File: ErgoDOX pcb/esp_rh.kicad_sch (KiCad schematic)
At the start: 6 parts

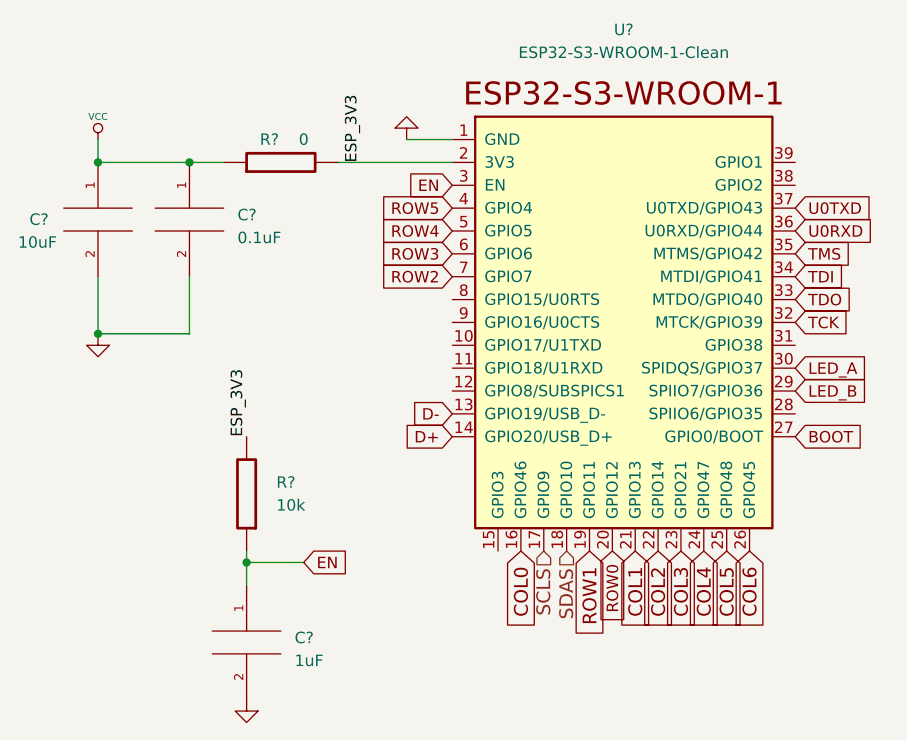
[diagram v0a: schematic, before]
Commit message: Create preliminary layout
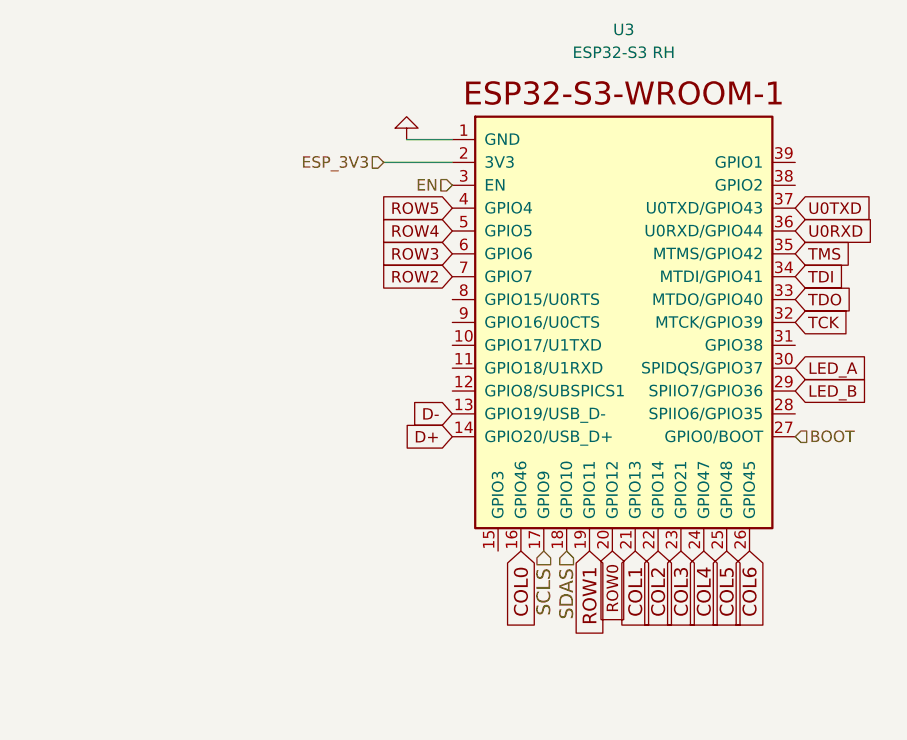
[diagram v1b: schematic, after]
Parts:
- removed C?: 1uF, symbol pspice:CAP
- removed C?: 10uF, symbol pspice:CAP
- removed C?: 0.1uF, symbol pspice:CAP
- removed R?: 10k, symbol component:RESISTOR
- removed R?: 0, symbol component:RESISTOR
- U3: renamed from U?; value ESP32-S3-WROOM-1-Clean -> ESP32-S3 RH
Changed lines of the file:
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@@
 (kicad_sch (version 20211123) (generator eeschema)
   (paper "A4")
-  (junction (at 119.38 83.82) (diameter 0) (color 0 0 0 0)
-  )
-  (junction (at 135.89 109.22) (diameter 0) (color 0 0 0 0)
-  )
-  (junction (at 119.38 64.77) (diameter 0) (color 0 0 0 0)
-  )
-  (junction (at 129.54 64.77) (diameter 0) (color 0 0 0 0)
-  )
-  (wire (pts (xy 129.54 77.47) (xy 129.54 83.82))
-    (stroke (width 0) (type default) (color 0 0 0 0))
-  )
-  (wire (pts (xy 119.38 62.23) (xy 119.38 64.77))
-    (stroke (width 0) (type default) (color 0 0 0 0))
-  )
-  (wire (pts (xy 129.54 64.77) (xy 133.35 64.77))
-    (stroke (width 0) (type default) (color 0 0 0 0))
-  )
-  (wire (pts (xy 135.89 109.22) (xy 135.89 111.76))
-    (stroke (width 0) (type default) (color 0 0 0 0))
-  )
-  (wire (pts (xy 146.05 64.77) (xy 158.75 64.77))
-    (stroke (width 0) (type default) (color 0 0 0 0))
-  )
-  (wire (pts (xy 129.54 83.82) (xy 119.38 83.82))
-    (stroke (width 0) (type default) (color 0 0 0 0))
-  )
-  (wire (pts (xy 135.89 107.95) (xy 135.89 109.22))
-    (stroke (width 0) (type default) (color 0 0 0 0))
-  )
-  (wire (pts (xy 119.38 83.82) (xy 119.38 77.47))
-    (stroke (width 0) (type default) (color 0 0 0 0))
-  )
-  (wire (pts (xy 119.38 64.77) (xy 129.54 64.77))
-    (stroke (width 0) (type default) (color 0 0 0 0))
-  )
-  (wire (pts (xy 135.89 109.22) (xy 142.24 109.22))
+  (wire (pts (xy 151.13 64.77) (xy 158.75 64.77))
     (stroke (width 0) (type default) (color 0 0 0 0))
   )
@@
     (stroke (width 0) (type default) (color 0 0 0 0))
   )
-  (label "ESP_3V3" (at 135.89 95.25 90)
-    (effects (font (size 1.27 1.27)) (justify left bottom))
-  )
-  (label "ESP_3V3" (at 148.59 64.77 90)
-    (effects (font (size 1.27 1.27)) (justify left bottom))
-  )
   (global_label "ROW0" (shape input) (at 176.53 107.95 270) (fields_autoplaced)
     (effects (font (size 1.27 1.27)) (justify right))
@@
     )
   )
-  (global_label "EN" (shape input) (at 142.24 109.22 0) (fields_autoplaced)
-    (effects (font (size 1.27 1.27)) (justify left))
-    (property "Intersheet References" "${INTERSHEET_REFS}" (id 0) (at 147.0437 109.1406 0)
-      (effects (font (size 1.27 1.27)) (justify left) hide)
-    )
-  )
-  (global_label "BOOT" (shape input) (at 196.85 95.25 0) (fields_autoplaced)
-    (effects (font (size 1.27 1.27)) (justify left))
-    (property "Intersheet References" "${INTERSHEET_REFS}" (id 0) (at 204.0728 95.1706 0)
-      (effects (font (size 1.27 1.27)) (justify left) hide)
-    )
-  )
   (global_label "TMS" (shape input) (at 196.85 74.93 0) (fields_autoplaced)
     (effects (font (size 1.27 1.27)) (justify left))
@@
     )
   )
-  (global_label "EN" (shape input) (at 158.75 67.31 180) (fields_autoplaced)
-    (effects (font (size 1.27 1.27)) (justify right))
-    (property "Intersheet References" "${INTERSHEET_REFS}" (id 0) (at 153.9463 67.2306 0)
-      (effects (font (size 1.27 1.27)) (justify right) hide)
-    )
-  )
   (global_label "COL5" (shape input) (at 189.23 107.95 270) (fields_autoplaced)
     (effects (font (size 1.524 1.524)) (justify right))
@@
     )
   )
+  (hierarchical_label "ESP_3V3" (shape input) (at 151.13 64.77 180)
+    (effects (font (size 1.27 1.27)) (justify right))
+  )
   (hierarchical_label "SDAS" (shape input) (at 171.45 107.95 270)
     (effects (font (size 1.524 1.524)) (justify right))
@@
     (effects (font (size 1.524 1.524)) (justify right))
   )
-  (symbol (lib_id "pspice:CAP") (at 135.89 118.11 0) (unit 1)
-    (in_bom yes) (on_board yes)
-    (property "Reference" "C?" (id 0) (at 141.224 117.6019 0)
-      (effects (font (size 1.27 1.27)) (justify left))
-    )
-    (property "Value" "1uF" (id 1) (at 141.224 120.1419 0)
-      (effects (font (size 1.27 1.27)) (justify left))
-    )
-    (property "Footprint" "" (id 2) (at 135.89 118.11 0)
-      (effects (font (size 1.27 1.27)) hide)
-    )
-    (property "Datasheet" "~" (id 3) (at 135.89 118.11 0)
-      (effects (font (size 1.27 1.27)) hide)
-    )
-    (pin "1")
-    (pin "2")
-  )
-  (symbol (lib_id "component:RESISTOR") (at 135.89 101.6 180) (unit 1)
-    (in_bom yes) (on_board yes) (fields_autoplaced)
-    (property "Reference" "R?" (id 0) (at 139.192 100.3299 0)
-      (effects (font (size 1.27 1.27)) (justify right))
-    )
-    (property "Value" "10k" (id 1) (at 139.192 102.8699 0)
-      (effects (font (size 1.27 1.27)) (justify right))
-    )
-    (property "Footprint" "" (id 2) (at 135.89 101.6 0)
-      (effects (font (size 1.27 1.27)) hide)
-    )
-    (property "Datasheet" "" (id 3) (at 135.89 101.6 0)
-      (effects (font (size 1.27 1.27)) hide)
-    )
-    (pin "1")
-    (pin "2")
-  )
-  (symbol (lib_id "component:GND") (at 119.38 85.09 0) (mirror y) (unit 1)
-    (in_bom yes) (on_board yes)
-    (property "Reference" "#PWR?" (id 0) (at 119.38 85.09 0)
-      (effects (font (size 0.762 0.762)) hide)
-    )
-    (property "Value" "GND" (id 1) (at 119.38 86.868 0)
-      (effects (font (size 0.762 0.762)) hide)
-    )
-    (property "Footprint" "" (id 2) (at 119.38 85.09 0)
-      (effects (font (size 1.524 1.524)) hide)
-    )
-    (property "Datasheet" "" (id 3) (at 119.38 85.09 0)
-      (effects (font (size 1.524 1.524)) hide)
-    )
-    (pin "1")
-  )
-  (symbol (lib_id "component:GND") (at 135.89 125.73 0) (mirror y) (unit 1)
-    (in_bom yes) (on_board yes)
-    (property "Reference" "#PWR?" (id 0) (at 135.89 125.73 0)
-      (effects (font (size 0.762 0.762)) hide)
-    )
-    (property "Value" "GND" (id 1) (at 135.89 127.508 0)
-      (effects (font (size 0.762 0.762)) hide)
-    )
-    (property "Footprint" "" (id 2) (at 135.89 125.73 0)
-      (effects (font (size 1.524 1.524)) hide)
-    )
-    (property "Datasheet" "" (id 3) (at 135.89 125.73 0)
-      (effects (font (size 1.524 1.524)) hide)
-    )
-    (pin "1")
-  )
-  (symbol (lib_id "pspice:CAP") (at 119.38 71.12 0) (unit 1)
-    (in_bom yes) (on_board yes)
-    (property "Reference" "C?" (id 0) (at 111.76 71.12 0)
-      (effects (font (size 1.27 1.27)) (justify left))
-    )
-    (property "Value" "10uF" (id 1) (at 110.49 73.66 0)
-      (effects (font (size 1.27 1.27)) (justify left))
-    )
-    (property "Footprint" "" (id 2) (at 119.38 71.12 0)
-      (effects (font (size 1.27 1.27)) hide)
-    )
-    (property "Datasheet" "~" (id 3) (at 119.38 71.12 0)
-      (effects (font (size 1.27 1.27)) hide)
-    )
-    (pin "1")
-    (pin "2")
-  )
-  (symbol (lib_id "component:RESISTOR") (at 139.7 64.77 90) (unit 1)
-    (in_bom yes) (on_board yes)
-    (property "Reference" "R?" (id 0) (at 138.43 62.23 90))
-    (property "Value" "0" (id 1) (at 142.24 62.23 90))
-    (property "Footprint" "" (id 2) (at 139.7 64.77 0)
-      (effects (font (size 1.27 1.27)) hide)
-    )
-    (property "Datasheet" "" (id 3) (at 139.7 64.77 0)
-      (effects (font (size 1.27 1.27)) hide)
-    )
-    (pin "1")
-    (pin "2")
+  (hierarchical_label "EN" (shape input) (at 158.75 67.31 180)
+    (effects (font (size 1.27 1.27)) (justify right))
+  )
+  (hierarchical_label "BOOT" (shape input) (at 196.85 95.25 0)
+    (effects (font (size 1.27 1.27)) (justify left))
   )
   (symbol (lib_id "Espressif:ESP32-S3-WROOM-1-Clean") (at 177.8 77.47 0) (unit 1)
     (in_bom yes) (on_board yes) (fields_autoplaced)
-    (property "Reference" "U?" (id 0) (at 177.8 50.038 0))
-    (property "Value" "ESP32-S3-WROOM-1-Clean" (id 1) (at 177.8 52.578 0))
+    (property "Reference" "U3" (id 0) (at 177.8 50.038 0))
+    (property "Value" "ESP32-S3 RH" (id 1) (at 177.8 52.578 0))
     (property "Footprint" "Espressif:ESP32-S3-WROOM-1" (id 2) (at 177.8 123.19 0)
       (effects (font (size 1.27 1.27)) hide)
@@
     (pin "9")
   )
-  (symbol (lib_id "component:VCC") (at 119.38 62.23 0) (unit 1)
-    (in_bom yes) (on_board yes)
-    (property "Reference" "#PWR?" (id 0) (at 119.38 59.69 0)
-      (effects (font (size 0.762 0.762)) hide)
-    )
-    (property "Value" "VCC" (id 1) (at 119.38 59.69 0)
-      (effects (font (size 0.762 0.762)))
-    )
-    (property "Footprint" "" (id 2) (at 119.38 62.23 0)
-      (effects (font (size 1.524 1.524)) hide)
-    )
-    (property "Datasheet" "" (id 3) (at 119.38 62.23 0)
-      (effects (font (size 1.524 1.524)) hide)
-    )
-    (pin "1")
-  )
   (symbol (lib_id "component:GND") (at 153.67 60.96 0) (mirror x) (unit 1)
     (in_bom yes) (on_board yes)
-    (property "Reference" "#PWR?" (id 0) (at 153.67 60.96 0)
+    (property "Reference" "#PWR035" (id 0) (at 153.67 60.96 0)
       (effects (font (size 0.762 0.762)) hide)
     )
@@
     (pin "1")
   )
-  (symbol (lib_id "pspice:CAP") (at 129.54 71.12 0) (unit 1)
-    (in_bom yes) (on_board yes)
-    (property "Reference" "C?" (id 0) (at 134.874 70.6119 0)
-      (effects (font (size 1.27 1.27)) (justify left))
-    )
-    (property "Value" "0.1uF" (id 1) (at 134.874 73.1519 0)
-      (effects (font (size 1.27 1.27)) (justify left))
-    )
-    (property "Footprint" "" (id 2) (at 129.54 71.12 0)
-      (effects (font (size 1.27 1.27)) hide)
-    )
-    (property "Datasheet" "~" (id 3) (at 129.54 71.12 0)
-      (effects (font (size 1.27 1.27)) hide)
-    )
-    (pin "1")
-    (pin "2")
-  )
 )

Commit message: First route of board
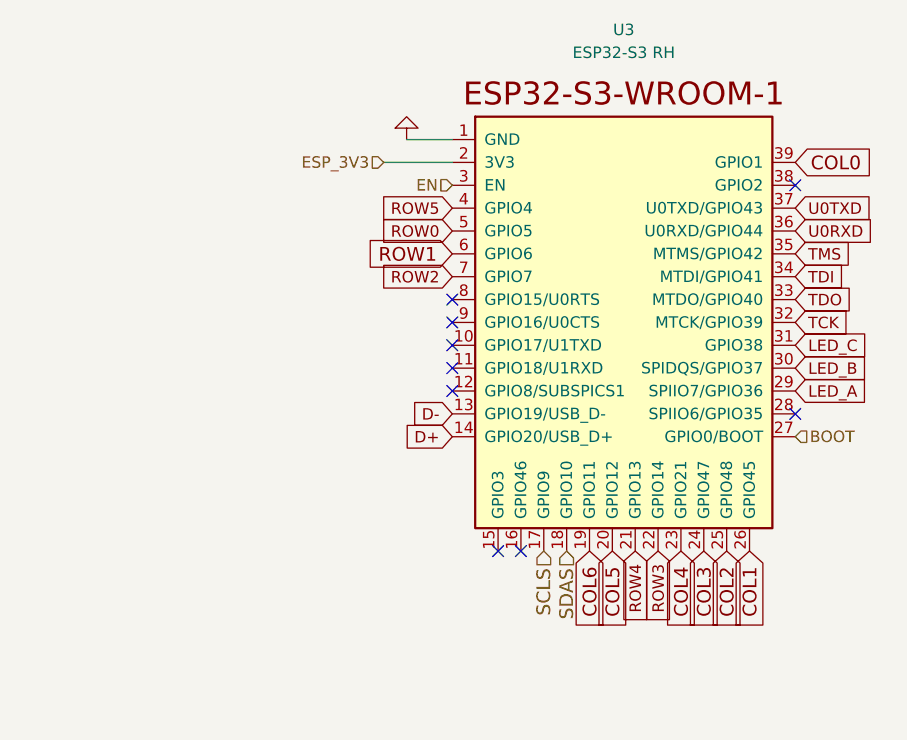
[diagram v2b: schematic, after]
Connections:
- net COL0: now also U3.39 (GPIO1); no longer U3.16 (GPIO46)
- net COL1: now also U3.26 (GPIO45); no longer U3.21 (GPIO13)
- net COL2: now also U3.25 (GPIO48); no longer U3.22 (GPIO14)
- net COL3: now also U3.24 (GPIO47); no longer U3.23 (GPIO21)
- net COL4: now also U3.23 (GPIO21); no longer U3.24 (GPIO47)
- net COL5: now also U3.20 (GPIO12); no longer U3.25 (GPIO48)
- net COL6: now also U3.19 (GPIO11); no longer U3.26 (GPIO45)
- net LED_A: now also U3.29 (SPIIO7/GPIO36); no longer U3.30 (SPIDQS/GPIO37)
- net LED_B: now also U3.30 (SPIDQS/GPIO37); no longer U3.29 (SPIIO7/GPIO36)
- net ROW0: now also U3.5 (GPIO5); no longer U3.20 (GPIO12)
- net ROW1: now also U3.6 (GPIO6); no longer U3.19 (GPIO11)
- net ROW3: now also U3.22 (GPIO14); no longer U3.6 (GPIO6)
- net ROW4: now also U3.21 (GPIO13); no longer U3.5 (GPIO5)
- net LED_C: now reaches U3.31 (GPIO38)
- no-connect marks 0 -> 9
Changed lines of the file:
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@@
 (kicad_sch (version 20211123) (generator eeschema)
   (paper "A4")
+  (no_connect (at 196.85 92.71))
+  (no_connect (at 158.75 80.01))
+  (no_connect (at 158.75 82.55))
+  (no_connect (at 166.37 107.95))
+  (no_connect (at 196.85 67.31))
+  (no_connect (at 158.75 85.09))
+  (no_connect (at 158.75 87.63))
+  (no_connect (at 163.83 107.95))
+  (no_connect (at 158.75 90.17))
   (wire (pts (xy 151.13 64.77) (xy 158.75 64.77))
     (stroke (width 0) (type default) (color 0 0 0 0))
@@
     (stroke (width 0) (type default) (color 0 0 0 0))
   )
-  (global_label "ROW0" (shape input) (at 176.53 107.95 270) (fields_autoplaced)
+  (global_label "LED_C" (shape input) (at 196.85 85.09 0) (fields_autoplaced)
+    (effects (font (size 1.27 1.27)) (justify left))
+    (property "Intersheet References" "${INTERSHEET_REFS}" (id 0) (at 204.859 85.0106 0)
+      (effects (font (size 1.27 1.27)) (justify left) hide)
+    )
+  )
+  (global_label "ROW0" (shape input) (at 158.75 72.39 180) (fields_autoplaced)
     (effects (font (size 1.27 1.27)) (justify right))
-    (property "Intersheet References" "${INTERSHEET_REFS}" (id 0) (at 176.4506 115.5356 90)
+    (property "Intersheet References" "${INTERSHEET_REFS}" (id 0) (at 151.1644 72.3106 0)
       (effects (font (size 1.27 1.27)) (justify right) hide)
     )
@@
     )
   )
-  (global_label "COL4" (shape input) (at 186.69 107.95 270) (fields_autoplaced)
+  (global_label "COL4" (shape input) (at 184.15 107.95 270) (fields_autoplaced)
     (effects (font (size 1.524 1.524)) (justify right))
-    (property "Intersheet References" "${INTERSHEET_REFS}" (id 0) (at 186.5948 116.5446 90)
+    (property "Intersheet References" "${INTERSHEET_REFS}" (id 0) (at 184.0548 116.5446 90)
       (effects (font (size 1.524 1.524)) (justify right) hide)
     )
   )
-  (global_label "COL5" (shape input) (at 189.23 107.95 270) (fields_autoplaced)
+  (global_label "COL5" (shape input) (at 176.53 107.95 270) (fields_autoplaced)
     (effects (font (size 1.524 1.524)) (justify right))
-    (property "Intersheet References" "${INTERSHEET_REFS}" (id 0) (at 189.1348 116.5446 90)
+    (property "Intersheet References" "${INTERSHEET_REFS}" (id 0) (at 176.4348 116.5446 90)
       (effects (font (size 1.524 1.524)) (justify right) hide)
     )
@@
     )
   )
-  (global_label "ROW1" (shape input) (at 173.99 107.95 270) (fields_autoplaced)
+  (global_label "ROW1" (shape input) (at 158.75 74.93 180) (fields_autoplaced)
     (effects (font (size 1.524 1.524)) (justify right))
-    (property "Intersheet References" "${INTERSHEET_REFS}" (id 0) (at 173.8948 117.0526 90)
+    (property "Intersheet References" "${INTERSHEET_REFS}" (id 0) (at 149.6474 74.8348 0)
       (effects (font (size 1.524 1.524)) (justify right) hide)
     )
@@
     )
   )
-  (global_label "ROW3" (shape input) (at 158.75 74.93 180) (fields_autoplaced)
+  (global_label "ROW3" (shape input) (at 181.61 107.95 270) (fields_autoplaced)
     (effects (font (size 1.27 1.27)) (justify right))
-    (property "Intersheet References" "${INTERSHEET_REFS}" (id 0) (at 151.1644 74.8506 0)
+    (property "Intersheet References" "${INTERSHEET_REFS}" (id 0) (at 181.5306 115.5356 90)
       (effects (font (size 1.27 1.27)) (justify right) hide)
     )
@@
     )
   )
-  (global_label "COL1" (shape input) (at 179.07 107.95 270) (fields_autoplaced)
+  (global_label "COL1" (shape input) (at 191.77 107.95 270) (fields_autoplaced)
     (effects (font (size 1.524 1.524)) (justify right))
-    (property "Intersheet References" "${INTERSHEET_REFS}" (id 0) (at 178.9748 116.5446 90)
+    (property "Intersheet References" "${INTERSHEET_REFS}" (id 0) (at 191.6748 116.5446 90)
       (effects (font (size 1.524 1.524)) (justify right) hide)
     )
   )
-  (global_label "LED_B" (shape input) (at 196.85 90.17 0) (fields_autoplaced)
+  (global_label "LED_B" (shape input) (at 196.85 87.63 0) (fields_autoplaced)
     (effects (font (size 1.27 1.27)) (justify left))
-    (property "Intersheet References" "${INTERSHEET_REFS}" (id 0) (at 204.859 90.0906 0)
+    (property "Intersheet References" "${INTERSHEET_REFS}" (id 0) (at 204.859 87.5506 0)
       (effects (font (size 1.27 1.27)) (justify left) hide)
     )
   )
-  (global_label "COL2" (shape input) (at 181.61 107.95 270) (fields_autoplaced)
+  (global_label "COL2" (shape input) (at 189.23 107.95 270) (fields_autoplaced)
     (effects (font (size 1.524 1.524)) (justify right))
-    (property "Intersheet References" "${INTERSHEET_REFS}" (id 0) (at 181.5148 116.5446 90)
+    (property "Intersheet References" "${INTERSHEET_REFS}" (id 0) (at 189.1348 116.5446 90)
       (effects (font (size 1.524 1.524)) (justify right) hide)
     )
@@
     )
   )
-  (global_label "COL6" (shape input) (at 191.77 107.95 270) (fields_autoplaced)
+  (global_label "COL6" (shape input) (at 173.99 107.95 270) (fields_autoplaced)
     (effects (font (size 1.524 1.524)) (justify right))
-    (property "Intersheet References" "${INTERSHEET_REFS}" (id 0) (at 191.6748 116.5446 90)
+    (property "Intersheet References" "${INTERSHEET_REFS}" (id 0) (at 173.8948 116.5446 90)
       (effects (font (size 1.524 1.524)) (justify right) hide)
     )
@@
     )
   )
-  (global_label "COL0" (shape input) (at 166.37 107.95 270) (fields_autoplaced)
+  (global_label "COL0" (shape input) (at 196.85 64.77 0) (fields_autoplaced)
+    (effects (font (size 1.524 1.524)) (justify left))
+    (property "Intersheet References" "${INTERSHEET_REFS}" (id 0) (at 205.4446 64.8652 0)
+      (effects (font (size 1.524 1.524)) (justify left) hide)
+    )
+  )
+  (global_label "LED_A" (shape input) (at 196.85 90.17 0) (fields_autoplaced)
+    (effects (font (size 1.27 1.27)) (justify left))
+    (property "Intersheet References" "${INTERSHEET_REFS}" (id 0) (at 204.6775 90.0906 0)
+      (effects (font (size 1.27 1.27)) (justify left) hide)
+    )
+  )
+  (global_label "COL3" (shape input) (at 186.69 107.95 270) (fields_autoplaced)
     (effects (font (size 1.524 1.524)) (justify right))
-    (property "Intersheet References" "${INTERSHEET_REFS}" (id 0) (at 166.2748 116.5446 90)
+    (property "Intersheet References" "${INTERSHEET_REFS}" (id 0) (at 186.5948 116.5446 90)
       (effects (font (size 1.524 1.524)) (justify right) hide)
     )
   )
-  (global_label "LED_A" (shape input) (at 196.85 87.63 0) (fields_autoplaced)
-    (effects (font (size 1.27 1.27)) (justify left))
-    (property "Intersheet References" "${INTERSHEET_REFS}" (id 0) (at 204.6775 87.5506 0)
-      (effects (font (size 1.27 1.27)) (justify left) hide)
-    )
-  )
-  (global_label "COL3" (shape input) (at 184.15 107.95 270) (fields_autoplaced)
-    (effects (font (size 1.524 1.524)) (justify right))
-    (property "Intersheet References" "${INTERSHEET_REFS}" (id 0) (at 184.0548 116.5446 90)
-      (effects (font (size 1.524 1.524)) (justify right) hide)
-    )
-  )
-  (global_label "ROW4" (shape input) (at 158.75 72.39 180) (fields_autoplaced)
+  (global_label "ROW4" (shape input) (at 179.07 107.95 270) (fields_autoplaced)
     (effects (font (size 1.27 1.27)) (justify right))
-    (property "Intersheet References" "${INTERSHEET_REFS}" (id 0) (at 151.1644 72.3106 0)
+    (property "Intersheet References" "${INTERSHEET_REFS}" (id 0) (at 178.9906 115.5356 90)
       (effects (font (size 1.27 1.27)) (justify right) hide)
     )
